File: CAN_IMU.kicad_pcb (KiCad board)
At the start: 4 copper layers, 77 x 61.5 mm, 37 parts, among them J1 USB_C_Receptacle_USB2.0_16P, J2 TAG SWD, J3 Conn_01x05, SW1 RST, SW2 SW_DIP_x02, U1 STM32G431CBTx, U2 USBLC6-2SC6, U3 SN74LVC1G126DBV, U4 TCAN3414, U5 TPS62172DSG

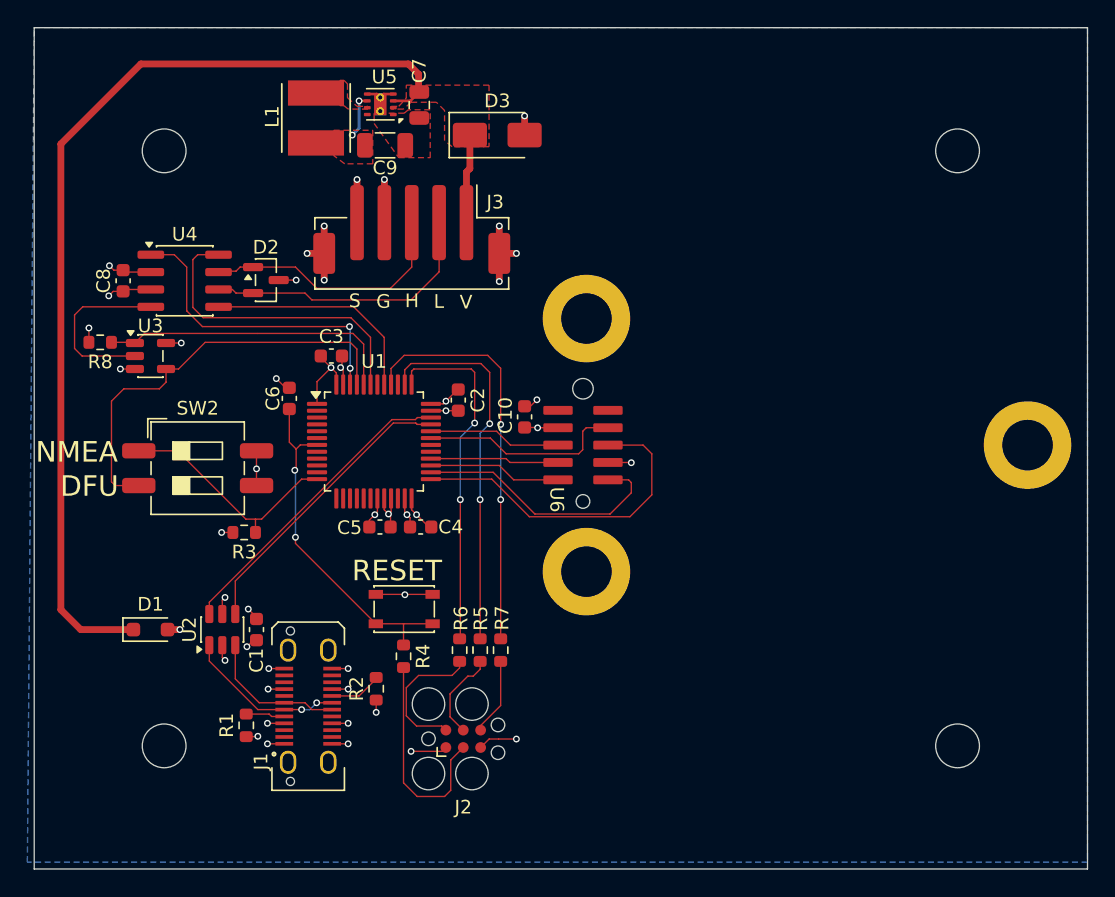
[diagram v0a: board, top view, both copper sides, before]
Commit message: Add onboard IMU and logo
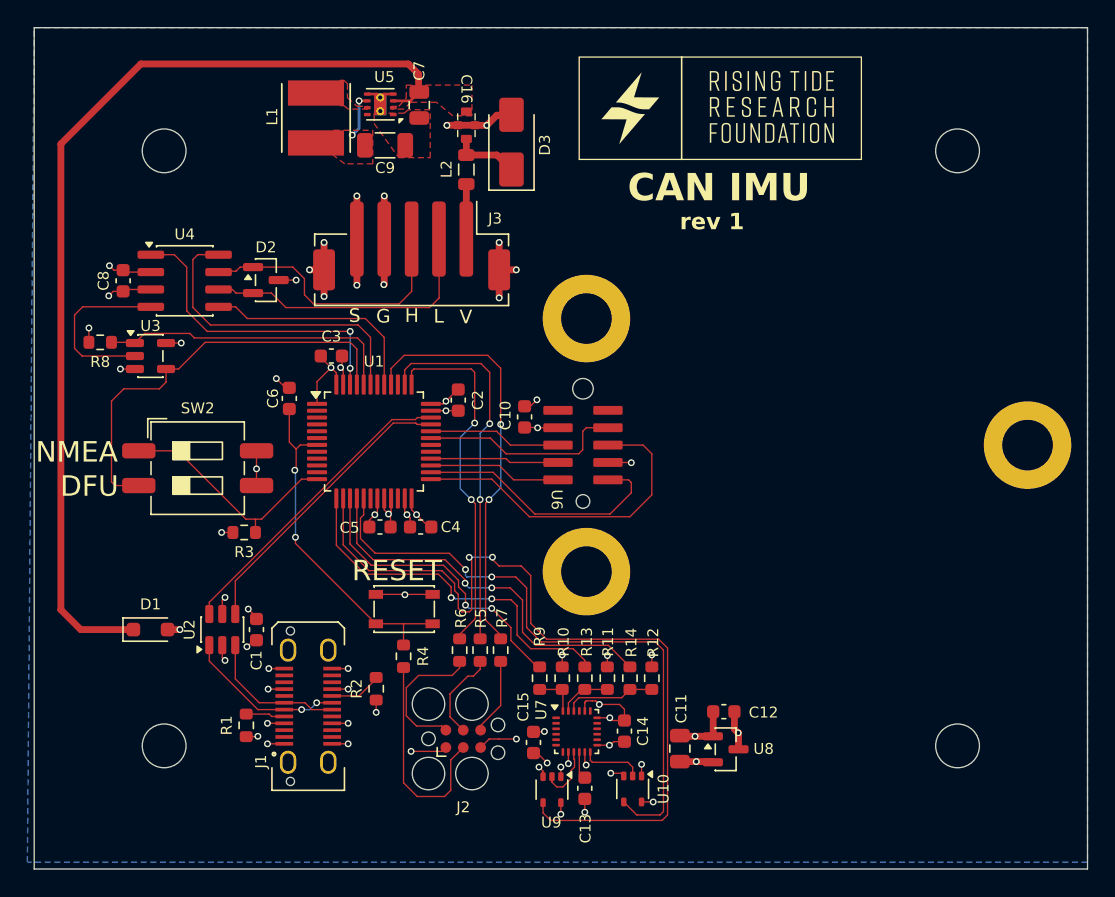
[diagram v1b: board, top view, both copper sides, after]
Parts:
- added C11: 10uF, Capacitor_SMD:C_0805_2012Metric, F.Cu at (87.2, 93.7)
- added C12: 1u, Capacitor_SMD:C_0603_1608Metric, F.Cu at (90.4, 91.0)
- added C13: 1u, Capacitor_SMD:C_0603_1608Metric, F.Cu at (80.2, 96.6)
- added C14: 1u, Capacitor_SMD:C_0603_1608Metric, F.Cu at (83.2, 92.4)
- added C15: 1u, Capacitor_SMD:C_0603_1608Metric, F.Cu at (76.5, 93.2)
- added C16: NFM21PC104R1E3D, RJMP_Misc:NFM21PC_Feedthrough_Cap, F.Cu at (71.6, 48.1)
- added L2: MPZ2012S601AT000, Inductor_SMD:L_0805_2012Metric, F.Cu at (71.6, 51.4)
- added R10: 5.1k, Resistor_SMD:R_0603_1608Metric, F.Cu at (78.6, 88.5)
- added R11: 5.1k, Resistor_SMD:R_0603_1608Metric, F.Cu at (81.9, 88.5)
- added R12: 5.1k, Resistor_SMD:R_0603_1608Metric, F.Cu at (85.2, 88.5)
- added R13: 5.1k, Resistor_SMD:R_0603_1608Metric, F.Cu at (80.2, 88.5)
- added R14: 5.1k, Resistor_SMD:R_0603_1608Metric, F.Cu at (83.5, 88.5)
- added R9: 5.1k, Resistor_SMD:R_0603_1608Metric, F.Cu at (77.0, 88.5)
- added U10: SN74AUP1T34DCK, Package_TO_SOT_SMD:SOT-353_SC-70-5, F.Cu at (83.8, 96.7)
- added U7: ICM-20948, Sensor_Motion:InvenSense_QFN-24_3x3mm_P0.4mm, F.Cu at (79.7, 92.5)
- added U8: MCP1700x-180xxTT, Package_TO_SOT_SMD:SOT-23, F.Cu at (90.5, 93.8)
- added U9: SN74AUP1T34DCK, Package_TO_SOT_SMD:SOT-353_SC-70-5, F.Cu at (77.8, 96.7)
- moved J3 1.20 mm to (67.6, 57.0)
- moved D3 1.16 mm to (74.9, 49.4), turned to 90 degrees
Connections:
- D3 pad 1: VBUS -> Net-(D3-K)
- J3 pad 1: VBUS -> Net-(J3-Pin_1)
- U1 pad 13: unconnected-(U1-PA5-Pad13) -> /ICM_SCLK
- U1 pad 14: unconnected-(U1-PA6-Pad14) -> /ICM_SDO
- U1 pad 15: unconnected-(U1-PA7-Pad15) -> /ICM_SDI
- U1 pad 16: unconnected-(U1-PB0-Pad16) -> /ICM_CSn
- U1 pad 17: unconnected-(U1-PB1-Pad17) -> /ICM_INT1
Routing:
- net /ICM_SDO: track 0.00 -> 61.5 mm, vias 0 -> 2
- net /ICM_INT1: track 0.00 -> 45.7 mm, vias 0 -> 2
- net GND: track 56.2 -> 85.1 mm, vias 31 -> 45
- net /ICM_CSn: track 0.00 -> 28.5 mm, vias 0 -> 2
- net /ICM_SCLK: track 0.00 -> 27.3 mm, vias 0 -> 2
- net /ICM_SDI: track 0.00 -> 22.2 mm, vias 0 -> 2
- net /Onboard IMU/ICM_CSn_r: track 0.00 -> 6.70 mm
- net VCC: track 29.8 -> 36.5 mm, vias 11 -> 15
- net VBUS: track 78.8 -> 72.3 mm
- net +1V8: track 0.00 -> 6.15 mm, vias 0 -> 5
- net Net-(D3-K): track 0.00 -> 5.50 mm
- net /Onboard IMU/ICM_INT1_1v8: track 0.00 -> 4.56 mm
- net /Onboard IMU/ICM_SDO_1v8: track 0.00 -> 4.27 mm
- net Net-(J3-Pin_1): track 0.00 -> 4.02 mm
- net /Onboard IMU/ICM_SCLK_r: track 0.00 -> 3.85 mm
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- added copper zone on In2.Cu, net +1V8
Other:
- board text added: "CAN IMU"
- board text added: "rev 1"

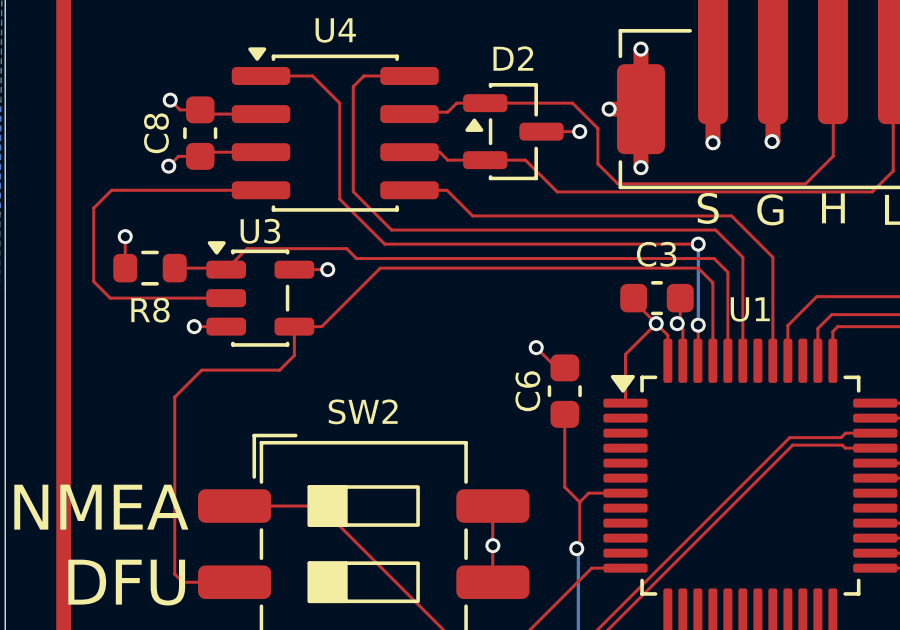
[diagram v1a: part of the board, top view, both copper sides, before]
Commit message: Add pull-down and series resistor to CAN_RX
Prevent shorting the buffer output when throwing the DIP switch
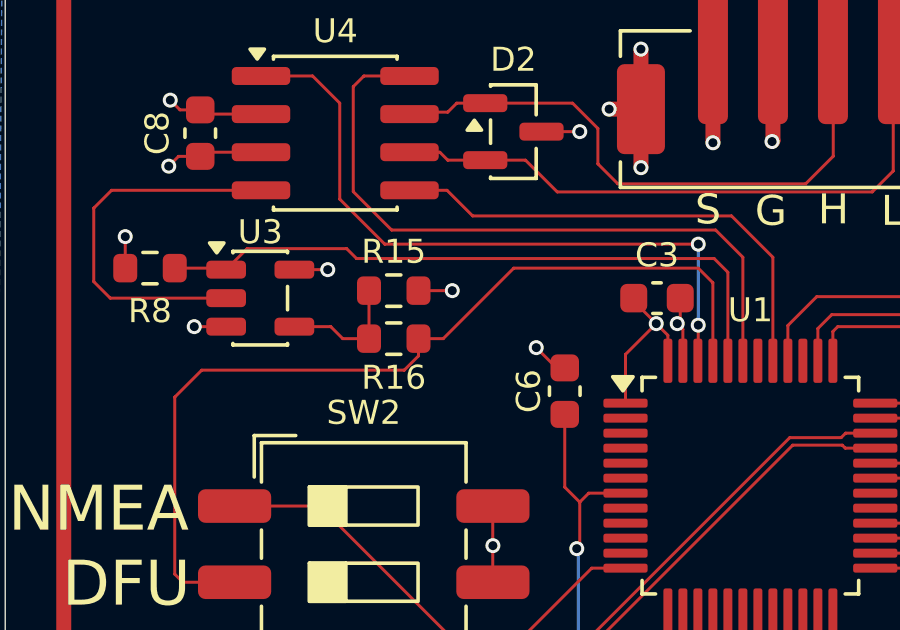
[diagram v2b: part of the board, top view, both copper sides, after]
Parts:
- added R15: 47k, Resistor_SMD:R_0603_1608Metric, F.Cu at (53.0, 64.8)
- added R16: 5.1k, Resistor_SMD:R_0603_1608Metric, F.Cu at (53.0, 66.3)
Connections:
- U3 pad 4: /CAN_RX-BOOT0 -> Net-(R15-Pad1)
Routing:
- net Net-(R15-Pad1): track 0.00 -> 4.25 mm
- net GND: track 85.1 -> 86.3 mm, vias 45 -> 46

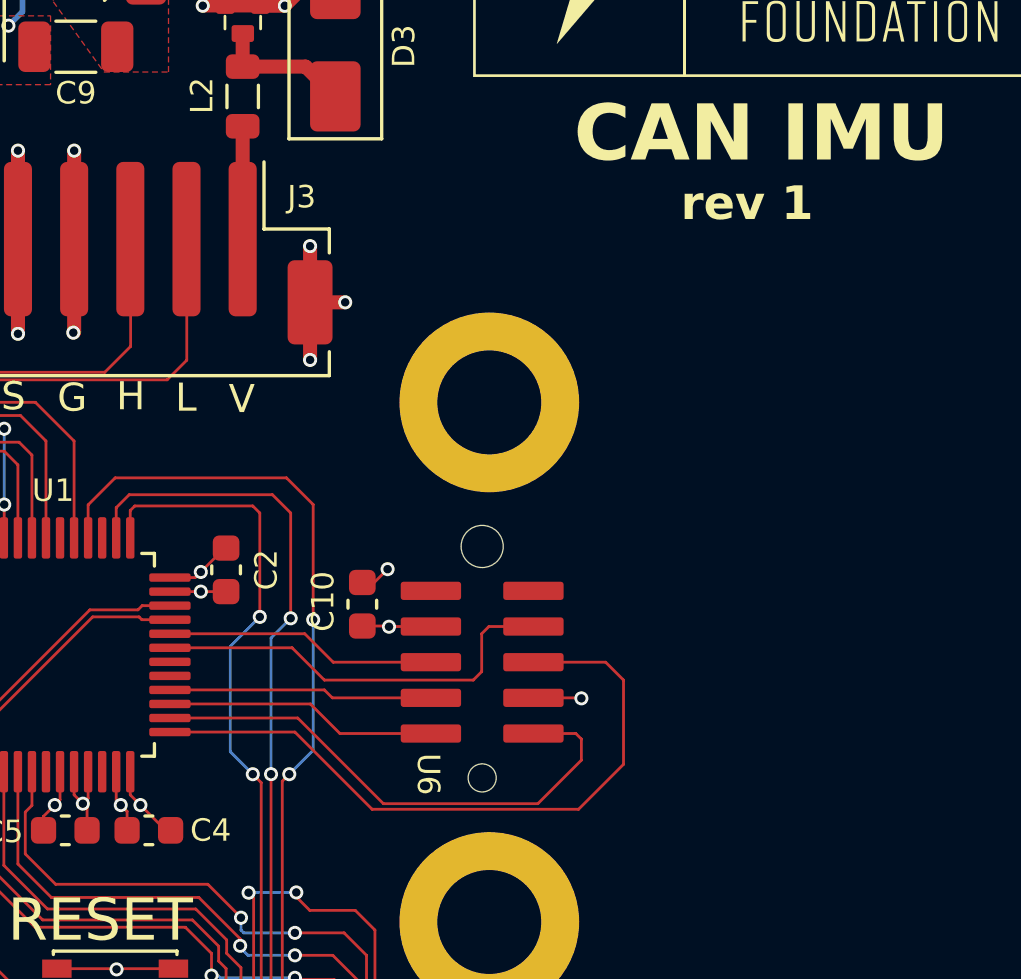
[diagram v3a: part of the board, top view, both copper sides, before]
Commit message: Rev 2 updates
- Fix microstrain connector pinout
- Update silkscreen rev
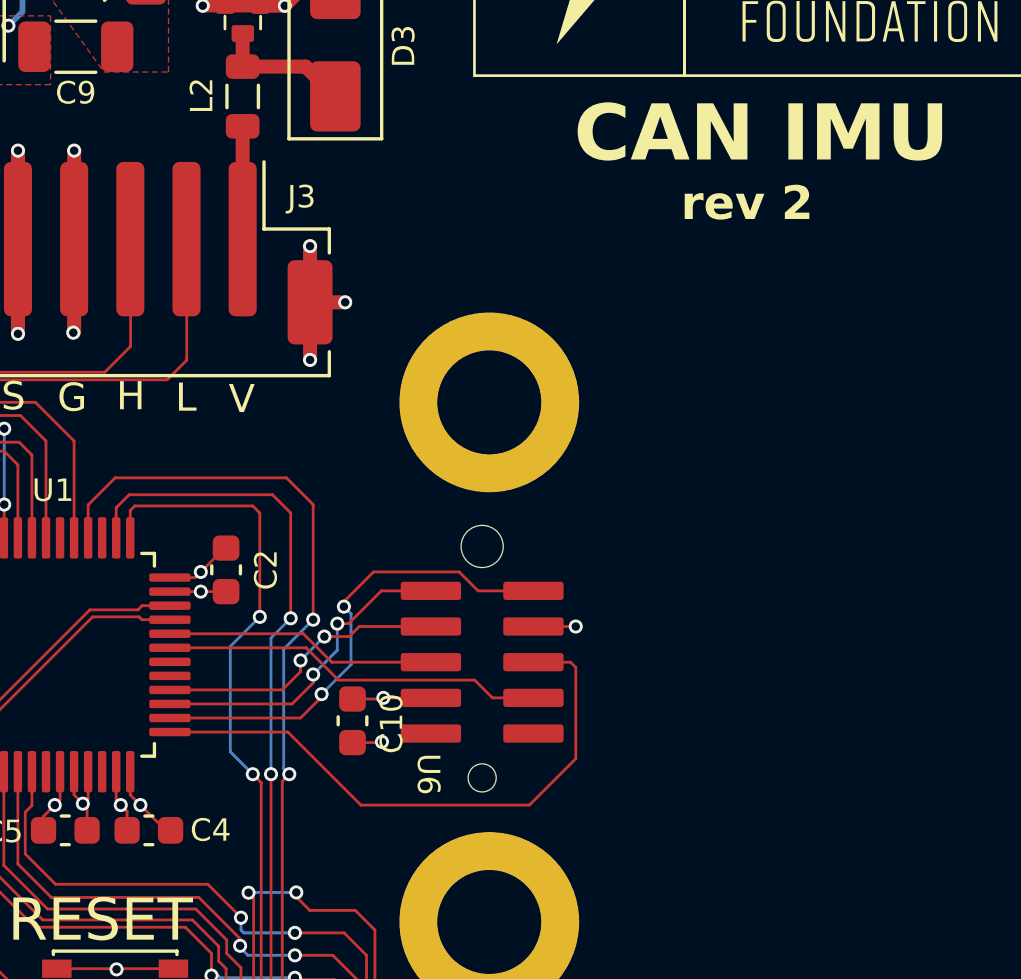
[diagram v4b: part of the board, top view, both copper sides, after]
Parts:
- moved C10 4.16 mm to (75.5, 73.6), turned to -90 degrees
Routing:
- net /IMU_GPIO3: track 24.4 -> 21.0 mm
- net /IMU_GPIO4: track 19.1 -> 17.1 mm, vias 0 -> 2
- net /IMU_GPIO2: track 9.73 -> 11.7 mm, vias 0 -> 2
- net /IMU_RX: track 15.0 -> 13.7 mm
- net /IMU_GPIO1: track 9.41 -> 10.5 mm, vias 0 -> 2
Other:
- board text added: "rev 2"
- board text removed: "rev 1"
